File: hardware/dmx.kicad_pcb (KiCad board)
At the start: 2 copper layers, 50 x 55 mm, 44 parts, among them P1 CON-SENSOR2, P2 BOOT, P3 DMXCON_2x3, SW1 TER, U1 XMC1XXX48, U2 DRILL, U3 DRILL, U4 DRILL, U5 DRILL, U6 ADM3485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

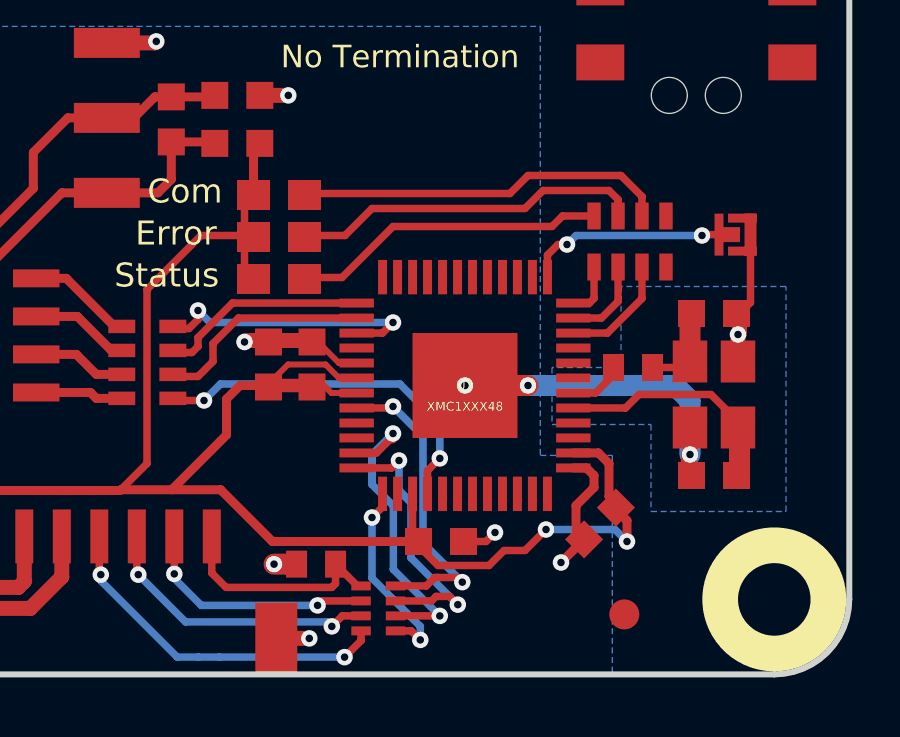
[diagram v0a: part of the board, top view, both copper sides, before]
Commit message: Change capacitor footprint(s) to C0402F
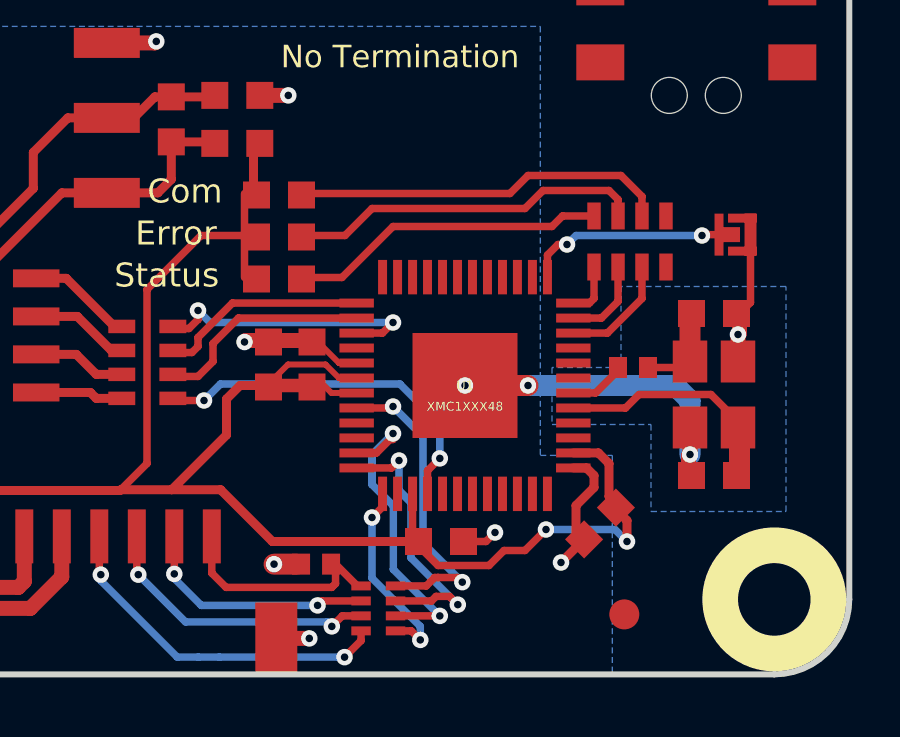
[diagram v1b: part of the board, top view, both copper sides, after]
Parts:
- C1, C2, C3, C4, C5, C6, C8, C9: footprint C0603F -> kicad-libraries:C0603F
- C10: footprint C0402E -> kicad-libraries:C0402F
- C7: footprint C0603E -> kicad-libraries:C0603E
- D1, D2, D3: footprint D0603E -> kicad-libraries:D0603F
- D4, D5: footprint DO-214AC -> kicad-libraries:DO-214AC
- L1: footprint WE-SL -> kicad-libraries:WE-SL
- P1: footprint CON-SENSOR2 -> kicad-libraries:CON-SENSOR2
- R1, R3, R4, R5: footprint R0603F -> kicad-libraries:R0603F
- R2: footprint R1206 -> kicad-libraries:R1206
- R9: footprint R0402E -> kicad-libraries:R0402F
- RP4: footprint 4X0402 -> kicad-libraries:4X0402
- U2, U3, U4, U5: footprint DRILL_NP -> kicad-libraries:DRILL_NP
- U6: footprint SOIC8 -> kicad-libraries:SOIC8
